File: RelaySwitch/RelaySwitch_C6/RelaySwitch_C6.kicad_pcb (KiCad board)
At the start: 2 copper layers, 53 x 53.5 mm, 46 parts, among them J1 AC_MAINS_IN, J3 LOAD_CH1, J4 LOAD_CH2, J5 SW1_INPUT, J6 SW2_INPUT, K1 G5Q-1-DC5, K2 G5Q-1-DC5, Q1 MMBT8050, Q2 MMBT8050, U1 HLK-2M05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

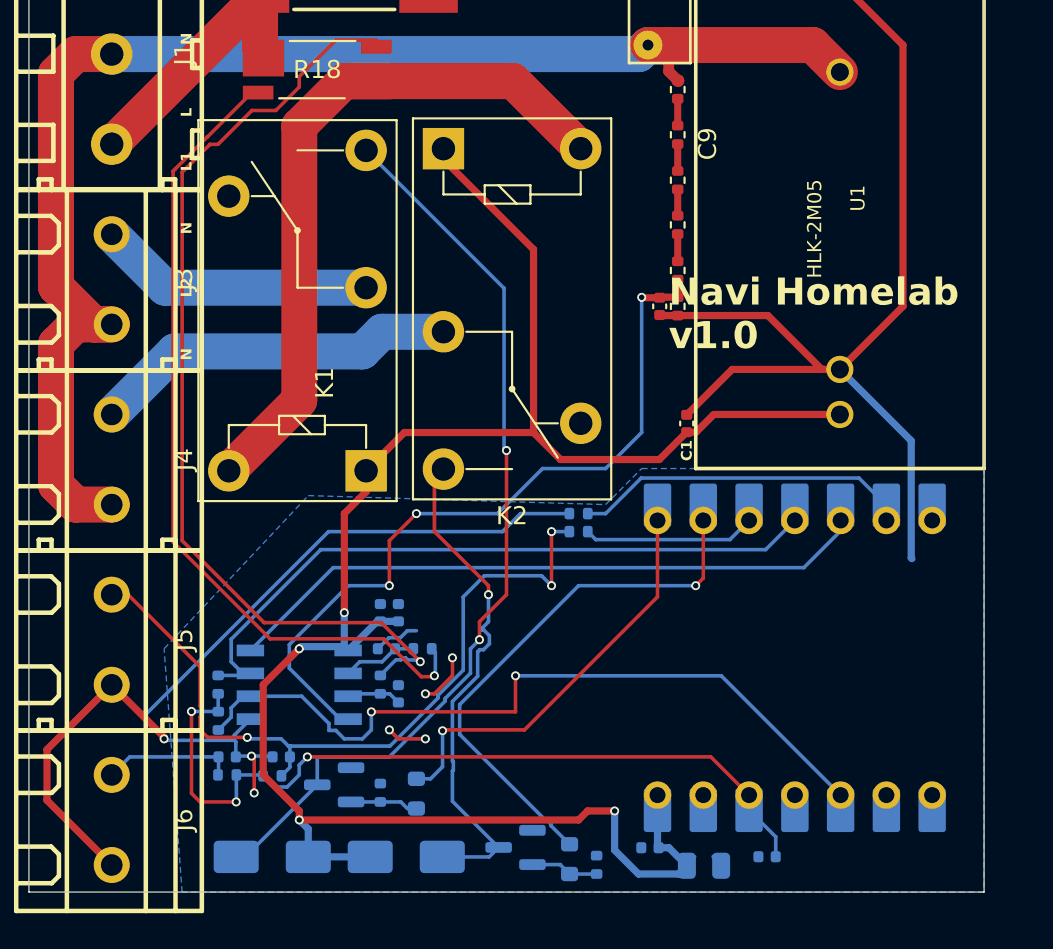
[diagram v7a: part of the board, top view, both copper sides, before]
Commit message: replaced the Q1 and 2 with Dual driver
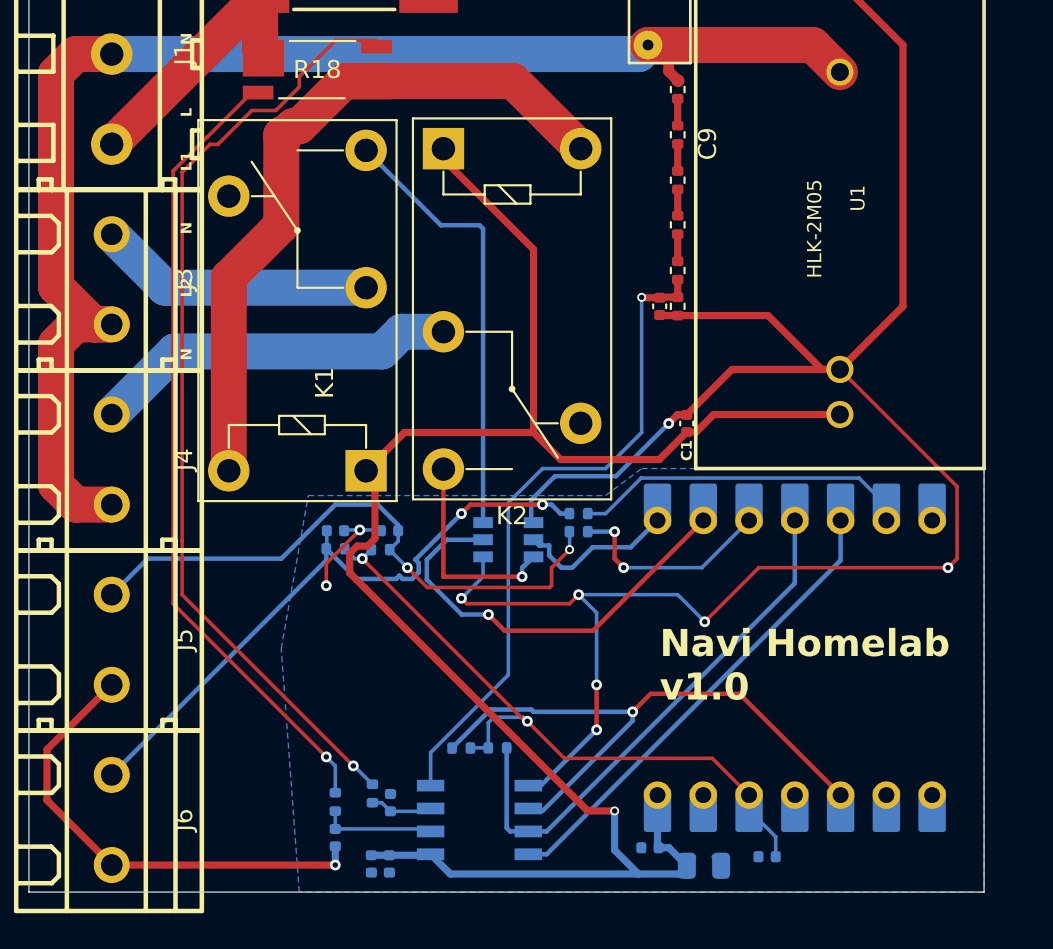
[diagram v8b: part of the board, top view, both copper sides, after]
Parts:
- removed D1, D2: 1N4007W, Diode_SMD:D_SMA
- removed Q1, Q2: MMBT8050, Package_TO_SOT_SMD:SOT-23
- removed R1, R3: 1k, Resistor_SMD:R_0603_1608Metric
- removed R2, R5: 10k, Resistor_SMD:R_0402_1005Metric
- added U3: NUD3124DMT1G, easyeda2kicad:SC-74-6_L3.0-W1.5-P0.95-LS2.8-BL, B.Cu at (168.6, 83.0)
- moved R11 15.9 mm to (168.0, 94.5), turned to 0 degrees
- moved C6 14.0 mm to (161.0, 100.9), turned to -90 degrees
- moved C4 13.9 mm to (162.0, 100.9), turned to -90 degrees
- moved C7 13.9 mm to (162.0, 82.5)
- moved C8 13.9 mm to (159.0, 82.5)
- moved R14 13.9 mm to (161.5, 83.5)
- moved R15 13.9 mm to (159.0, 83.5)
- moved R12 13.6 mm to (166.0, 94.5), turned to 180 degrees
- moved U5 12.5 mm to (167.0, 98.5), turned to 0 degrees
- moved C10 10.9 mm to (159.0, 99.5), turned to -90 degrees
- moved R19 9.78 mm to (159.0, 97.5), turned to 90 degrees
- moved C11 6.06 mm to (162.1, 97.5)
- moved R20 6.06 mm to (161.1, 97.0)
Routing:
- net GND: track 116.9 -> 172.4 mm, vias 7 -> 10
- net Net-(K1-COIL_2): track 51.3 -> 24.6 mm, vias 2 -> 0
- net Net-(K2-COIL_2): track 28.2 -> 11.7 mm
- net /RELAY_CH1_IN: track 23.0 -> 8.93 mm, vias 1 -> 0
- net /HLW_SEL: track 36.9 -> 26.3 mm
- net Net-(C7-Pad1): track 42.5 -> 33.4 mm, vias 3 -> 2
- net /HLW_CF: track 42.8 -> 33.7 mm, vias 2 -> 1
- net +5V: track 110.4 -> 101.4 mm, vias 4 -> 1
- net /HLW_CF1: track 38.4 -> 29.7 mm
- net +3V3: track 45.1 -> 36.8 mm, vias 3 -> 2
- net /RELAY_CH2_IN: track 30.0 -> 23.7 mm
- net Net-(U5-V2P): track 42.1 -> 37.0 mm, vias 3 -> 1
- net Net-(Q2-B): track 3.78 -> 0.00 mm
- net Net-(Q1-B): track 3.78 -> 0.00 mm
- net Net-(C8-Pad1): track 37.8 -> 35.4 mm, vias 0 -> 2
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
